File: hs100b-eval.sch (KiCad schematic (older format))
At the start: 44 parts, among them IC1 HS-100B, J1 SPKR, J2 MIC, J3 RADIO_DATA, SW1 MUTE_REC, SW2 MUTE_PLAY, SW3 VOL_DN, SW4 VOL_UP

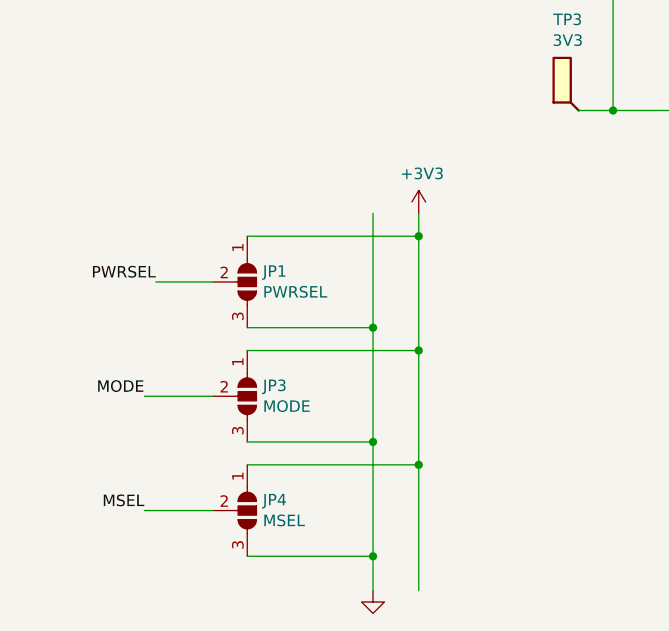
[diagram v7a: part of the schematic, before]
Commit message: Move to DIP switches for config
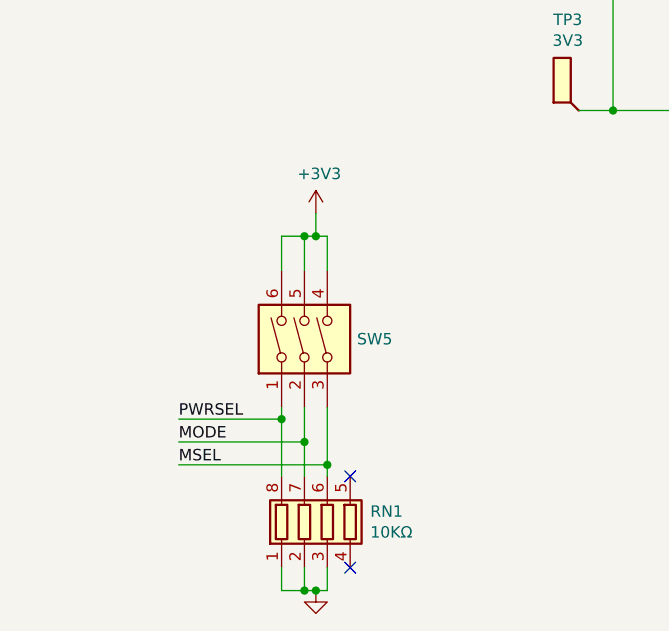
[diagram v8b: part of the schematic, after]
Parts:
- removed JP1: PWRSEL, Connector_PinHeader_2.54mm:PinHeader_1x03_P2.54mm_Vertical, symbol Jumper:SolderJumper_3_Open
- removed JP3: MODE, Connector_PinHeader_2.54mm:PinHeader_1x03_P2.54mm_Vertical, symbol Jumper:SolderJumper_3_Open
- removed JP4: MSEL, Connector_PinHeader_2.54mm:PinHeader_1x03_P2.54mm_Vertical, symbol Jumper:SolderJumper_3_Open
- added RN1: 10KΩ, Resistor_SMD:R_Array_Concave_4x0402, symbol Device:R_Pack04
- added SW5: SW_DIP_x03, Diptronics:DMR, symbol Switch:SW_DIP_x03
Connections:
- net +3V3: now also SW5.4, SW5.5, SW5.6
- net GND: now also RN1.1 (R1.1), RN1.2 (R2.1), RN1.3 (R3.1)
- net MODE: now also RN1.7 (R2.2), SW5.2
- net MSEL: now also RN1.6 (R3.2), SW5.3
- net PWRSEL: now also RN1.8 (R1.2), SW5.1
- no-connect marks 8 -> 10
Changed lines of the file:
@@
-$EndComp
-$Comp
-L Jumper:SolderJumper_3_Open JP1
-U 1 1 6063CF0E
-P 2000 5000
-F 0 "JP1" V 1954 5068 50  0000 L CNN
-F 1 "PWRSEL" V 2045 5068 50  0000 L CNN
-F 2 "Connector_PinHeader_2.54mm:PinHeader_1x03_P2.54mm_Vertical" H 2000 5000 50  0001 C CNN
-F 3 "https://www.amphenol-icc.com/media/wysiwyg/files/documentation/datasheet/boardwiretoboard/bwb_econostik_254headers.pdf" H 2000 5000 50  0001 C CNN
-F 4 "0.1" H 1954 5168 50  0001 C CNN "Price"
-F 5 "649-1012937890301BLF" H 1954 5168 50  0001 C CNN "Vendor Part #"
-F 6 "Mouser" H 1954 5168 50  0001 C CNN "Vendor"
-	1    2000 5000
-	0    1    1    0
 $EndComp
 $Comp
 L power:+3V3 #PWR05
 U 1 1 6064094B
-P 2750 4700
-F 0 "#PWR05" H 2750 4550 50  0001 C CNN
-F 1 "+3V3" H 2765 4873 50  0000 C CNN
-F 2 "" H 2750 4700 50  0001 C CNN
-F 3 "" H 2750 4700 50  0001 C CNN
-	1    2750 4700
+P 2300 4700
+F 0 "#PWR05" H 2300 4550 50  0001 C CNN
+F 1 "+3V3" H 2315 4873 50  0000 C CNN
+F 2 "" H 2300 4700 50  0001 C CNN
+F 3 "" H 2300 4700 50  0001 C CNN
+	1    2300 4700
 	1    0    0    -1
 $EndComp
@@
 L power:GND #PWR04
 U 1 1 60642C2C
-P 2550 6350
-F 0 "#PWR04" H 2550 6100 50  0001 C CNN
-F 1 "GND" H 2555 6177 50  0001 C CNN
-F 2 "" H 2550 6350 50  0001 C CNN
-F 3 "" H 2550 6350 50  0001 C CNN
-	1    2550 6350
-	1    0    0    -1
-$EndComp
-$Comp
-L Jumper:SolderJumper_3_Open JP3
-U 1 1 60645210
-P 2000 5500
-F 0 "JP3" V 1954 5568 50  0000 L CNN
-F 1 "MODE" V 2045 5568 50  0000 L CNN
-F 2 "Connector_PinHeader_2.54mm:PinHeader_1x03_P2.54mm_Vertical" H 2000 5500 50  0001 C CNN
-F 3 "https://www.amphenol-icc.com/media/wysiwyg/files/documentation/datasheet/boardwiretoboard/bwb_econostik_254headers.pdf" H 2000 5500 50  0001 C CNN
-F 4 "0.1" H 1954 5668 50  0001 C CNN "Price"
-F 5 "649-1012937890301BLF" H 1954 5668 50  0001 C CNN "Vendor Part #"
-F 6 "Mouser" H 1954 5668 50  0001 C CNN "Vendor"
-	1    2000 5500
-	0    1    1    0
-$EndComp
-$Comp
-L Jumper:SolderJumper_3_Open JP4
-U 1 1 6064583B
-P 2000 6000
-F 0 "JP4" V 1954 6068 50  0000 L CNN
-F 1 "MSEL" V 2045 6068 50  0000 L CNN
-F 2 "Connector_PinHeader_2.54mm:PinHeader_1x03_P2.54mm_Vertical" H 2000 6000 50  0001 C CNN
-F 3 "https://www.amphenol-icc.com/media/wysiwyg/files/documentation/datasheet/boardwiretoboard/bwb_econostik_254headers.pdf" H 2000 6000 50  0001 C CNN
-F 4 "0.1" H 1954 6168 50  0001 C CNN "Price"
-F 5 "649-1012937890301BLF" H 1954 6168 50  0001 C CNN "Vendor Part #"
-F 6 "Mouser" H 1954 6168 50  0001 C CNN "Vendor"
-	1    2000 6000
-	0    1    1    0
+P 2300 6350
+F 0 "#PWR04" H 2300 6100 50  0001 C CNN
+F 1 "GND" H 2305 6177 50  0001 C CNN
+F 2 "" H 2300 6350 50  0001 C CNN
+F 3 "" H 2300 6350 50  0001 C CNN
+	1    2300 6350
+	1    0    0    -1
 $EndComp
 $Comp
@@
 Text Label 5350 2750 1    50   ~ 0
 MODE
-Text Label 1600 5000 2    50   ~ 0
+Text Label 1700 5600 0    50   ~ 0
 PWRSEL
-Text Label 1550 5500 2    50   ~ 0
+Text Label 1700 5700 0    50   ~ 0
 MODE
 Text Label 5150 2750 1    50   ~ 0
 MSEL
-Text Label 1550 6000 2    50   ~ 0
+Text Label 1700 5800 0    50   ~ 0
 MSEL
 Text Label 4050 4750 2    50   ~ 0
@@
 	9400 1950 9400 2350
 Wire Wire Line
-	1600 5000 1850 5000
-Wire Wire Line
-	2000 4800 2750 4800
-Wire Wire Line
-	2750 4800 2750 4700
-Wire Wire Line
-	2000 5300 2750 5300
-Wire Wire Line
-	2750 5300 2750 4800
-Wire Wire Line
-	2000 5800 2750 5800
-Wire Wire Line
-	2000 6200 2550 6200
-Wire Wire Line
-	2550 6200 2550 6350
-Wire Wire Line
-	2000 5700 2550 5700
-Wire Wire Line
-	2550 5700 2550 6200
-Wire Wire Line
-	2000 5200 2550 5200
-Wire Wire Line
-	1550 5500 1850 5500
-Wire Wire Line
-	1550 6000 1850 6000
+	2300 4800 2300 4700
 Wire Wire Line
 	7200 2200 7200 2300
@@
 Wire Wire Line
 	8900 5500 8700 5500
-Wire Wire Line
-	2550 4700 2550 5200
-Wire Wire Line
-	2550 5200 2550 5700
-Wire Wire Line
-	2750 5800 2750 6350
-Wire Wire Line
-	2750 5300 2750 5800
 Wire Wire Line
 	1350 3250 1350 3550
@@
 Connection ~ 9400 6200
 Connection ~ 9400 2350
-Connection ~ 2750 4800
-Connection ~ 2750 5300
-Connection ~ 2550 6200
-Connection ~ 2550 5700
 Connection ~ 6750 2600
 Connection ~ 6350 2600
@@
 Connection ~ 7200 2300
 Connection ~ 8850 3150
-Connection ~ 2550 5200
-Connection ~ 2750 5800
 Connection ~ 4850 5450
 Connection ~ 4950 5450
@@
 Wire Wire Line
 	1350 3550 1350 3600
+$Comp
+L Switch:SW_DIP_x03 SW5
+U 1 1 6081E826
+P 2350 5250
+F 0 "SW5" V 2350 5120 50  0000 R CNN
+F 1 "SW_DIP_x03" V 2305 5120 50  0001 R CNN
+F 2 "Diptronics:DMR" H 2350 5250 50  0001 C CNN
+F 3 "https://www.mouser.com/datasheet/2/910/374_DM-1544377.pdf" H 2350 5250 50  0001 C CNN
+F 4 "1.72" H 2350 5250 50  0001 C CNN "Price"
+F 5 "Mouser" H 2350 5250 50  0001 C CNN "Vendor"
+F 6 "113-DMR03V" H 2350 5250 50  0001 C CNN "Vendor Part #"
+	1    2350 5250
+	0    -1   -1   0
+$EndComp
+Wire Wire Line
+	2150 4950 2150 4800
+Wire Wire Line
+	2150 4800 2250 4800
+Wire Wire Line
+	2250 4950 2250 4800
+Connection ~ 2250 4800
+Wire Wire Line
+	2250 4800 2300 4800
+Wire Wire Line
+	2350 4950 2350 4800
+Wire Wire Line
+	2350 4800 2300 4800
+Connection ~ 2300 4800
+$Comp
+L Device:R_Pack04 RN1
+U 1 1 6083D634
+P 2350 6050
+F 0 "RN1" H 2538 6096 50  0000 L CNN
+F 1 "10KΩ" H 2538 6005 50  0000 L CNN
+F 2 "Resistor_SMD:R_Array_Concave_4x0402" V 2625 6050 50  0001 C CNN
+F 3 "https://www.mouser.com/datasheet/2/54/CAT10-1954944.pdf" H 2350 6050 50  0001 C CNN
+F 4 "0.10" H 2350 6050 50  0001 C CNN "Price"
+F 5 "Mouser" H 2350 6050 50  0001 C CNN "Vendor"
+F 6 "652-CAT10A-103J2LF" H 2350 6050 50  0001 C CNN "Vendor Part #"
+	1    2350 6050
+	1    0    0    -1
+$EndComp
+Wire Wire Line
+	2150 6250 2150 6350
+Wire Wire Line
+	2150 6350 2250 6350
+Wire Wire Line
+	2250 6250 2250 6350
+Connection ~ 2250 6350
+Wire Wire Line
+	2250 6350 2300 6350
+Wire Wire Line
+	2350 6250 2350 6350
+Wire Wire Line
+	2350 6350 2300 6350
+Connection ~ 2300 6350
+NoConn ~ 2450 6250
+NoConn ~ 2450 5850
+Wire Wire Line
+	2150 5550 2150 5600
+Wire Wire Line
+	2250 5550 2250 5700
+Wire Wire Line
+	2350 5550 2350 5800
+Connection ~ 2150 5600
+Wire Wire Line
+	2150 5600 2150 5850
+Wire Wire Line
+	1700 5700 2250 5700
+Connection ~ 2250 5700
+Wire Wire Line
+	2250 5700 2250 5850
+Wire Wire Line
+	1700 5800 2350 5800
+Connection ~ 2350 5800
+Wire Wire Line
+	2350 5800 2350 5850
+Wire Wire Line
+	1700 5600 2150 5600
 $EndSCHEMATC
